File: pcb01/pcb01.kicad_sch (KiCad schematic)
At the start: 58 parts, among them J1 DIN41612_02x32_AC, J11 Conn_01x09, J2 Jmp_UART_Irq, J3 Conn_01x09_Socket, J4 Conn_01x08_Socket, J5 UART, J6 Conn_01x02_Socket, J7 Jmp_Irq, J8 Jmp_NMI, J9 Ram1 Enable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

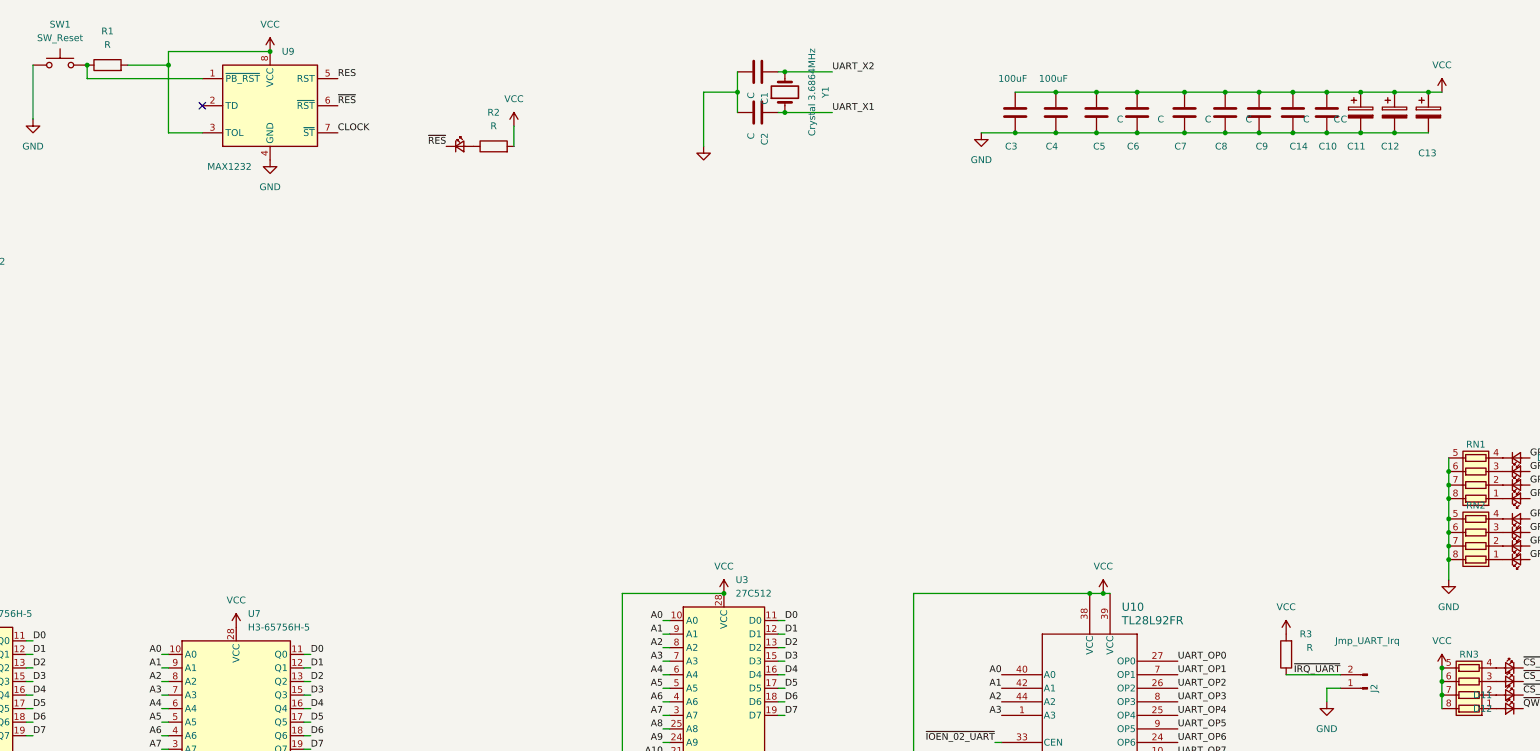
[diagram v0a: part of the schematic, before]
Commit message: annotate values & add reset pull-up
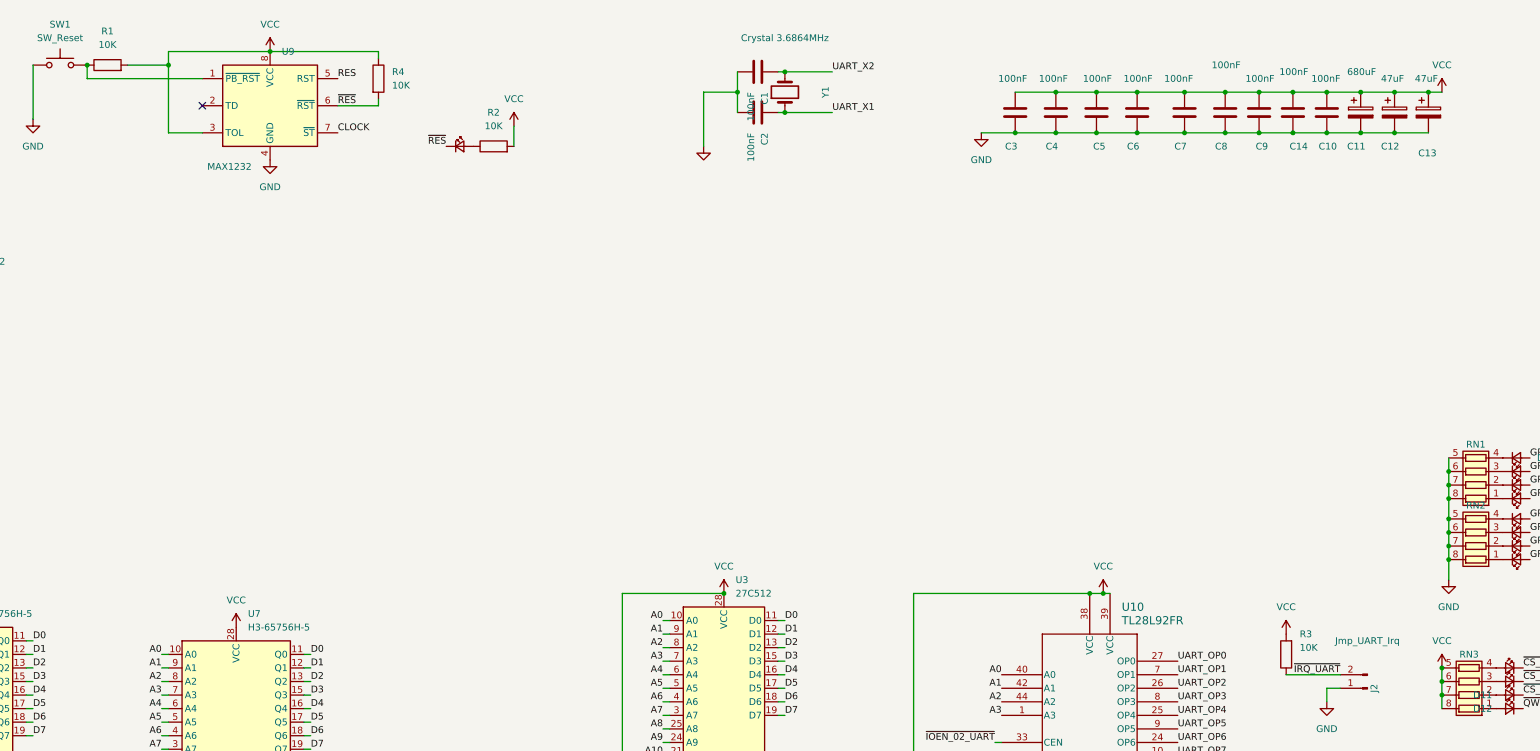
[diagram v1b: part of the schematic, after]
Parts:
- added R4: 10K, Resistor_THT:R_Axial_DIN0207_L6.3mm_D2.5mm_P7.62mm_Horizontal, symbol Device:R
- C1, C10, C14, C2, C5, C6, C7, C8, C9: value C -> 100nF
- C11: value C_Polarized -> 680uF
- C12, C13: value C_Polarized -> 47uF
- C3, C4: value 100uF -> 100nF
- R1, R2, R3: value R -> 10K
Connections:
- net VCC: now also R4.1
- net ~{RES}: now also R4.2
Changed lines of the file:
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@@
     (stroke (width 0) (type default))
   )
+  (wire (pts (xy 167.64 33.02) (xy 175.26 33.02))
+    (stroke (width 0) (type default))
+  )
   (wire (pts (xy 302.26 30.48) (xy 309.88 30.48))
     (stroke (width 0) (type default))
@@
     (stroke (width 0) (type default))
   )
+  (wire (pts (xy 175.26 24.13) (xy 175.26 22.86))
+    (stroke (width 0) (type default))
+  )
+  (wire (pts (xy 154.94 22.86) (xy 175.26 22.86))
+    (stroke (width 0) (type default))
+  )
   (wire (pts (xy 177.8 231.14) (xy 177.8 270.51))
     (stroke (width 0) (type default))
@@
     (stroke (width 0) (type default))
   )
+  (wire (pts (xy 175.26 33.02) (xy 175.26 31.75))
+    (stroke (width 0) (type default))
+  )
   (wire (pts (xy 58.42 154.94) (xy 57.15 154.94))
     (stroke (width 0) (type default))
@@
       (effects (font (size 1.27 1.27)) (justify left))
     )
-    (property "Value" "C" (at 348.615 35.56 0)
+    (property "Value" "100nF" (at 337.82 27.94 0)
       (effects (font (size 1.27 1.27)) (justify left))
     )
@@
       (effects (font (size 1.27 1.27)))
     )
-    (property "Value" "R" (at 196.85 36.83 90)
+    (property "Value" "10K" (at 196.85 36.83 90)
       (effects (font (size 1.27 1.27)))
     )
@@
       (effects (font (size 1.27 1.27)) (justify left))
     )
-    (property "Value" "C" (at 354.33 35.56 0)
+    (property "Value" "100nF" (at 344.17 26.67 0)
       (effects (font (size 1.27 1.27)) (justify left))
     )
@@
       (effects (font (size 1.27 1.27)) (justify left))
     )
-    (property "Value" "C" (at 313.69 35.56 0)
+    (property "Value" "100nF" (at 307.34 27.94 0)
       (effects (font (size 1.27 1.27)) (justify left))
     )
@@
       (effects (font (size 1.27 1.27)) (justify right))
     )
-    (property "Value" "R" (at 349.25 134.62 0)
+    (property "Value" "10K" (at 347.98 134.62 0)
       (effects (font (size 1.27 1.27)) (justify right))
     )
@@
       (effects (font (size 1.27 1.27)) (justify left))
     )
-    (property "Value" "C" (at 337.82 35.56 0)
+    (property "Value" "100nF" (at 331.47 25.4 0)
       (effects (font (size 1.27 1.27)) (justify left))
     )
@@
   )
   (symbol (lib_id "Device:Crystal") (at 251.46 30.48 90) (unit 1)
-    (in_bom yes) (on_board yes) (dnp no) (fields_autoplaced)
+    (in_bom yes) (on_board yes) (dnp no)
     (property "Reference" "Y1" (at 259.08 30.48 0)
       (effects (font (size 1.27 1.27)))
     )
-    (property "Value" "Crystal 3.6864MHz" (at 256.54 30.48 0)
+    (property "Value" "Crystal 3.6864MHz" (at 251.46 20.32 90)
       (effects (font (size 1.27 1.27)))
     )
@@
       (effects (font (size 1.27 1.27)) (justify left))
     )
-    (property "Value" "100uF" (at 291.465 27.94 0)
+    (property "Value" "100nF" (at 291.465 27.94 0)
       (effects (font (size 1.27 1.27)) (justify left))
     )
@@
       (effects (font (size 1.27 1.27)) (justify right))
     )
-    (property "Value" "C" (at 356.87 35.56 0)
+    (property "Value" "100nF" (at 355.6 27.94 0)
       (effects (font (size 1.27 1.27)) (justify right))
     )
@@
       (effects (font (size 1.27 1.27)) (justify left))
     )
-    (property "Value" "100uF" (at 299.085 27.94 0)
+    (property "Value" "100nF" (at 299.085 27.94 0)
       (effects (font (size 1.27 1.27)) (justify left))
     )
@@
       (effects (font (size 1.27 1.27)) (justify left))
     )
-    (property "Value" "C_Polarized" (at 374.015 38.735 0)
-      (effects (font (size 1.27 1.27)) (justify left) hide)
+    (property "Value" "47uF" (at 369.57 27.94 0)
+      (effects (font (size 1.27 1.27)) (justify left))
     )
     (property "Footprint" "Capacitor_THT:CP_Radial_D4.0mm_P2.00mm" (at 373.0752 38.1 0)
@@
       (effects (font (size 1.27 1.27)))
     )
-    (property "Value" "R" (at 124.46 21.59 90)
+    (property "Value" "10K" (at 124.46 21.59 90)
       (effects (font (size 1.27 1.27)))
     )
@@
       (effects (font (size 1.27 1.27)) (justify left))
     )
-    (property "Value" "C" (at 245.11 38.1 0)
+    (property "Value" "100nF" (at 245.11 38.1 0)
       (effects (font (size 1.27 1.27)) (justify left))
     )
@@
       (effects (font (size 1.27 1.27)) (justify left))
     )
-    (property "Value" "C" (at 321.31 35.56 0)
+    (property "Value" "100nF" (at 314.96 27.94 0)
       (effects (font (size 1.27 1.27)) (justify left))
     )
@@
       (effects (font (size 1.27 1.27)) (justify left))
     )
-    (property "Value" "C" (at 245.11 30.48 0)
+    (property "Value" "100nF" (at 245.11 30.48 0)
       (effects (font (size 1.27 1.27)) (justify left))
     )
@@
       (effects (font (size 1.27 1.27)) (justify left))
     )
-    (property "Value" "C_Polarized" (at 365.76 40.005 0)
-      (effects (font (size 1.27 1.27)) (justify left) hide)
+    (property "Value" "47uF" (at 363.22 27.94 0)
+      (effects (font (size 1.27 1.27)) (justify left))
     )
     (property "Footprint" "Capacitor_THT:CP_Radial_D4.0mm_P2.00mm" (at 366.7252 38.1 0)
@@
       (effects (font (size 1.27 1.27)) (justify left))
     )
-    (property "Value" "C" (at 330.2 35.56 0)
+    (property "Value" "100nF" (at 322.58 27.94 0)
       (effects (font (size 1.27 1.27)) (justify left))
     )
@@
       (effects (font (size 1.27 1.27)) (justify left))
     )
-    (property "Value" "C_Polarized" (at 358.14 42.545 0)
-      (effects (font (size 1.27 1.27)) (justify left) hide)
+    (property "Value" "680uF" (at 356.87 26.67 0)
+      (effects (font (size 1.27 1.27)) (justify left))
     )
     (property "Footprint" "Capacitor_THT:CP_Radial_D8.0mm_P5.00mm" (at 360.3752 38.1 0)
@@
         )
       )
+    )
+  )
+  (symbol (lib_id "Device:R") (at 175.26 27.94 0) (unit 1)
+    (in_bom yes) (on_board yes) (dnp no) (fields_autoplaced)
+    (property "Reference" "R4" (at 177.8 26.67 0)
+      (effects (font (size 1.27 1.27)) (justify left))
+    )
+    (property "Value" "10K" (at 177.8 29.21 0)
+      (effects (font (size 1.27 1.27)) (justify left))
+    )
+    (property "Footprint" "Resistor_THT:R_Axial_DIN0207_L6.3mm_D2.5mm_P7.62mm_Horizontal" (at 173.482 27.94 90)
+      (effects (font (size 1.27 1.27)) hide)
+    )
+    (property "Datasheet" "~" (at 175.26 27.94 0)
+      (effects (font (size 1.27 1.27)) hide)
+    )
+    (pin "2")
+    (pin "1")
+    (instances
+      (project "pcb01"
+        (path "/a9a73dc6-7f92-4458-9da8-49621d12e480"
+          (reference "R4") (unit 1)
+        )
+      )

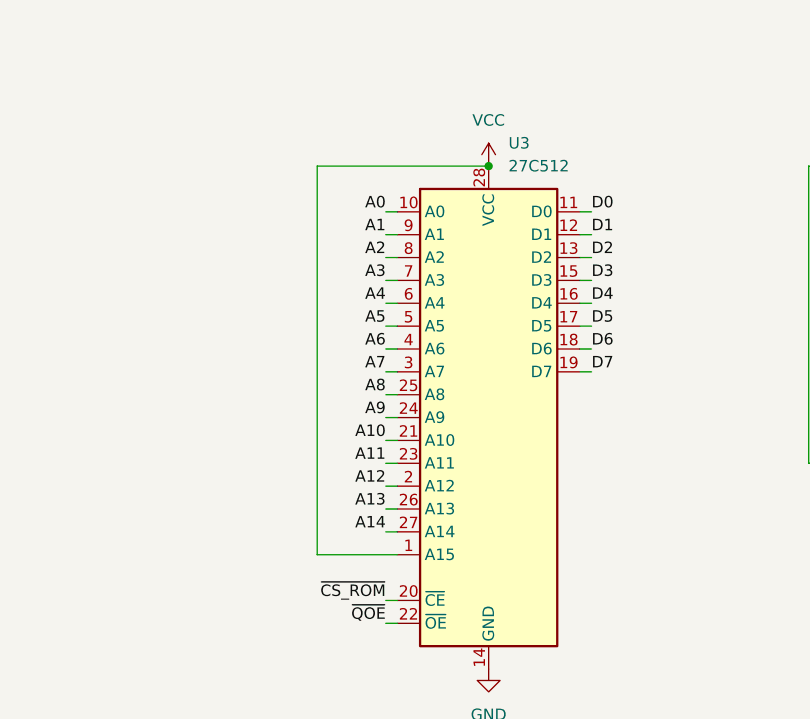
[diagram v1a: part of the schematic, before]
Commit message: connect rom A15
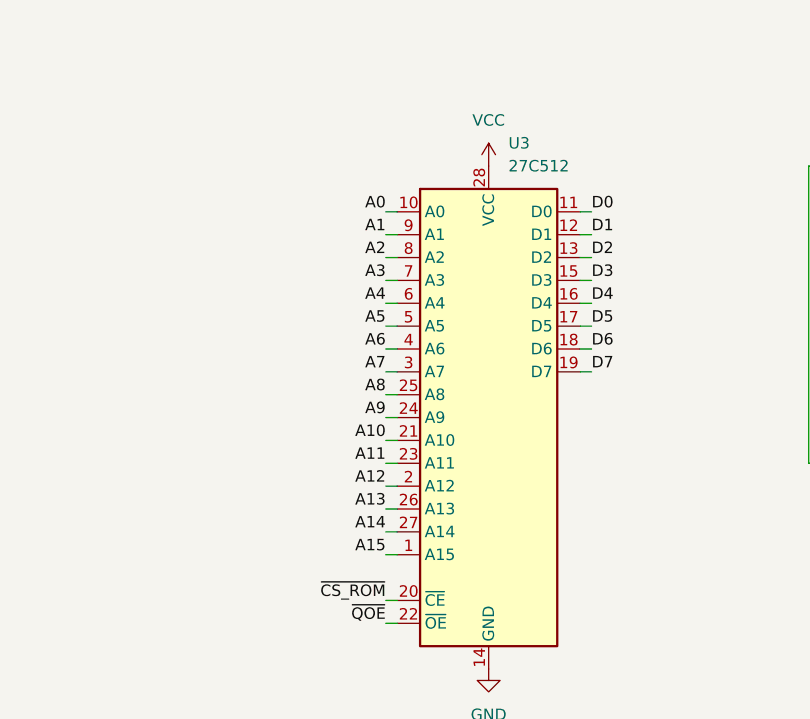
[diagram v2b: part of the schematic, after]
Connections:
- net A15: now also U3.1 (A15)
- net VCC: no longer U3.1 (A15)
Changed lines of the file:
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@@
   (junction (at 334.01 38.1) (diameter 0) (color 0 0 0 0)
-  )
-  (junction (at 240.03 124.46) (diameter 0) (color 0 0 0 0)
   )
   (junction (at 154.94 22.86) (diameter 0) (color 0 0 0 0)
@@
     (stroke (width 0) (type default))
   )
+  (wire (pts (xy 228.6 167.64) (xy 229.87 167.64))
+    (stroke (width 0) (type default))
+  )
   (wire (pts (xy 58.42 162.56) (xy 57.15 162.56))
     (stroke (width 0) (type default))
@@
     (stroke (width 0) (type default))
   )
-  (wire (pts (xy 220.98 124.46) (xy 240.03 124.46))
-    (stroke (width 0) (type default))
-  )
   (wire (pts (xy 82.55 148.59) (xy 83.82 148.59))
     (stroke (width 0) (type default))
@@
     (stroke (width 0) (type default))
   )
-  (wire (pts (xy 220.98 167.64) (xy 220.98 124.46))
-    (stroke (width 0) (type default))
-  )
   (wire (pts (xy 58.42 127) (xy 57.15 127))
     (stroke (width 0) (type default))
@@
     (stroke (width 0) (type default))
   )
-  (wire (pts (xy 220.98 167.64) (xy 229.87 167.64))
-    (stroke (width 0) (type default))
-  )
   (wire (pts (xy 134.62 161.29) (xy 135.89 161.29))
     (stroke (width 0) (type default))
@@
     (effects (font (size 1.27 1.27)) (justify right bottom))
   )
+  (label "A15" (at 228.6 167.64 180) (fields_autoplaced)
+    (effects (font (size 1.27 1.27)) (justify right bottom))
+  )
